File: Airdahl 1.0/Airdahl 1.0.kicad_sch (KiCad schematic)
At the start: 31 parts, among them J1 Conn_ARM_JTAG_SWD_20, SW1 SW_MEC_5E, U1 STM32F446RETx, X2 ABS25-32.768KHZ-6-T, Y1 ABM3B-8.000MHZ-12-D1X-T

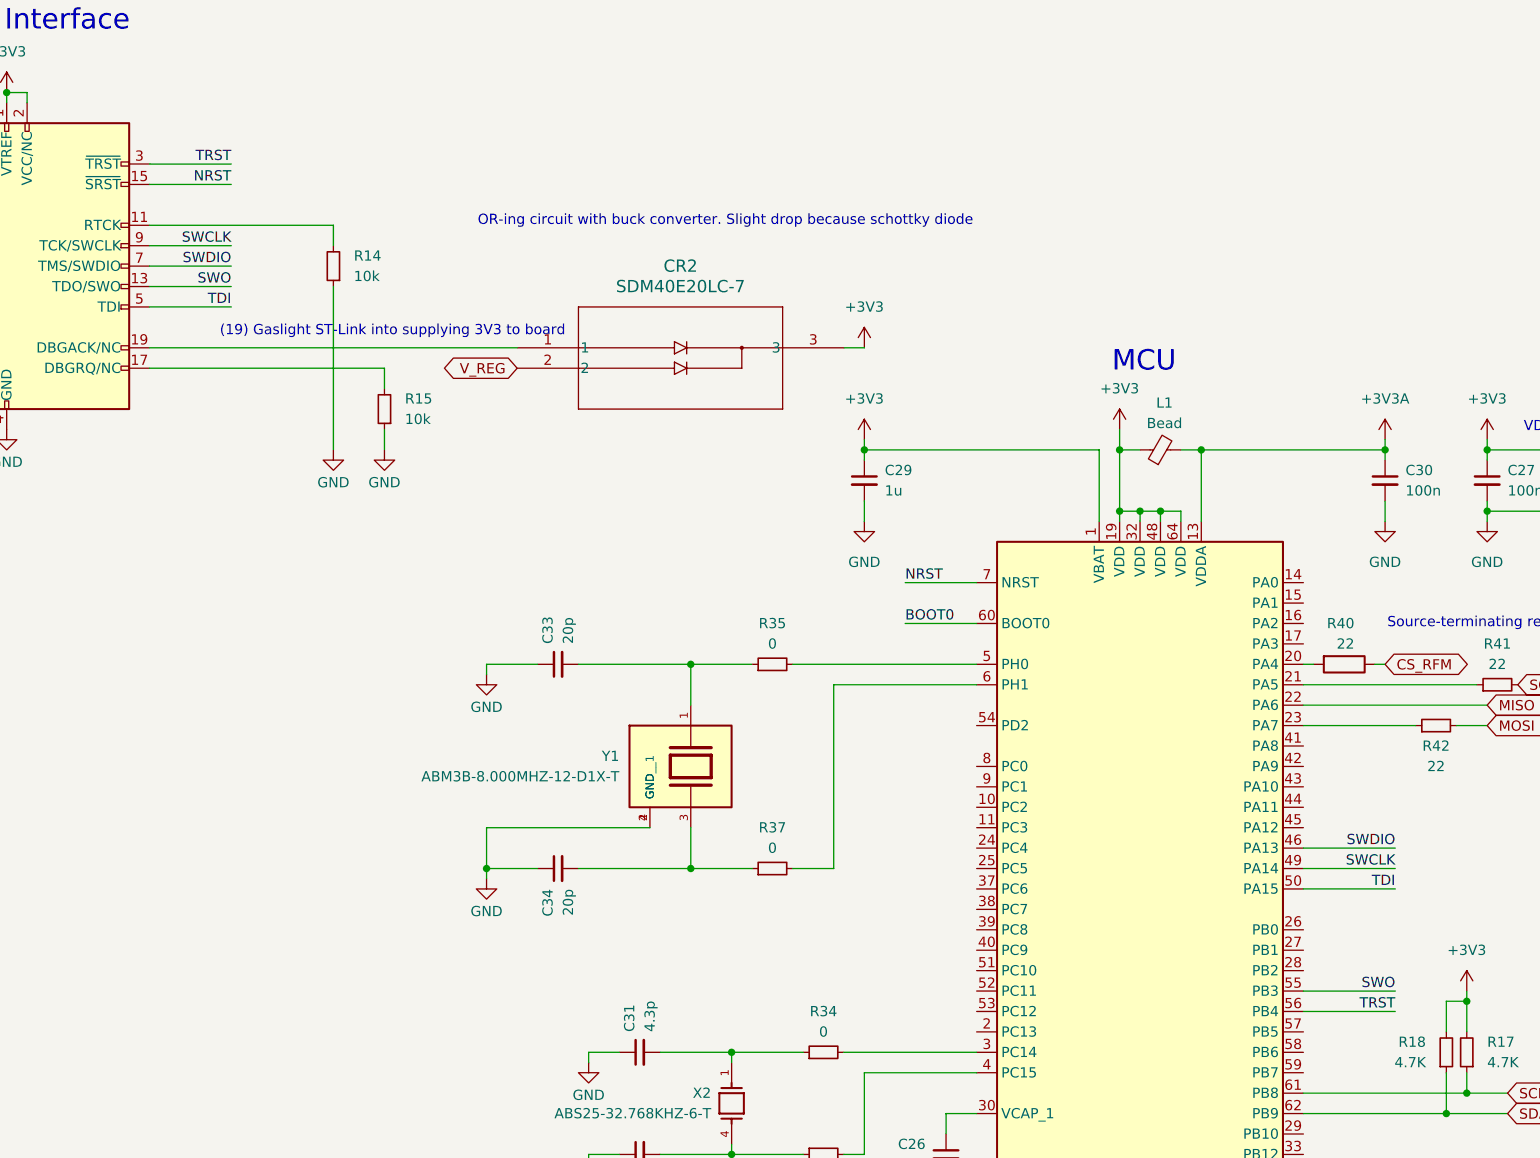
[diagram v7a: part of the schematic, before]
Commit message: added 5v buck, h bridge IC, updated jtag connections
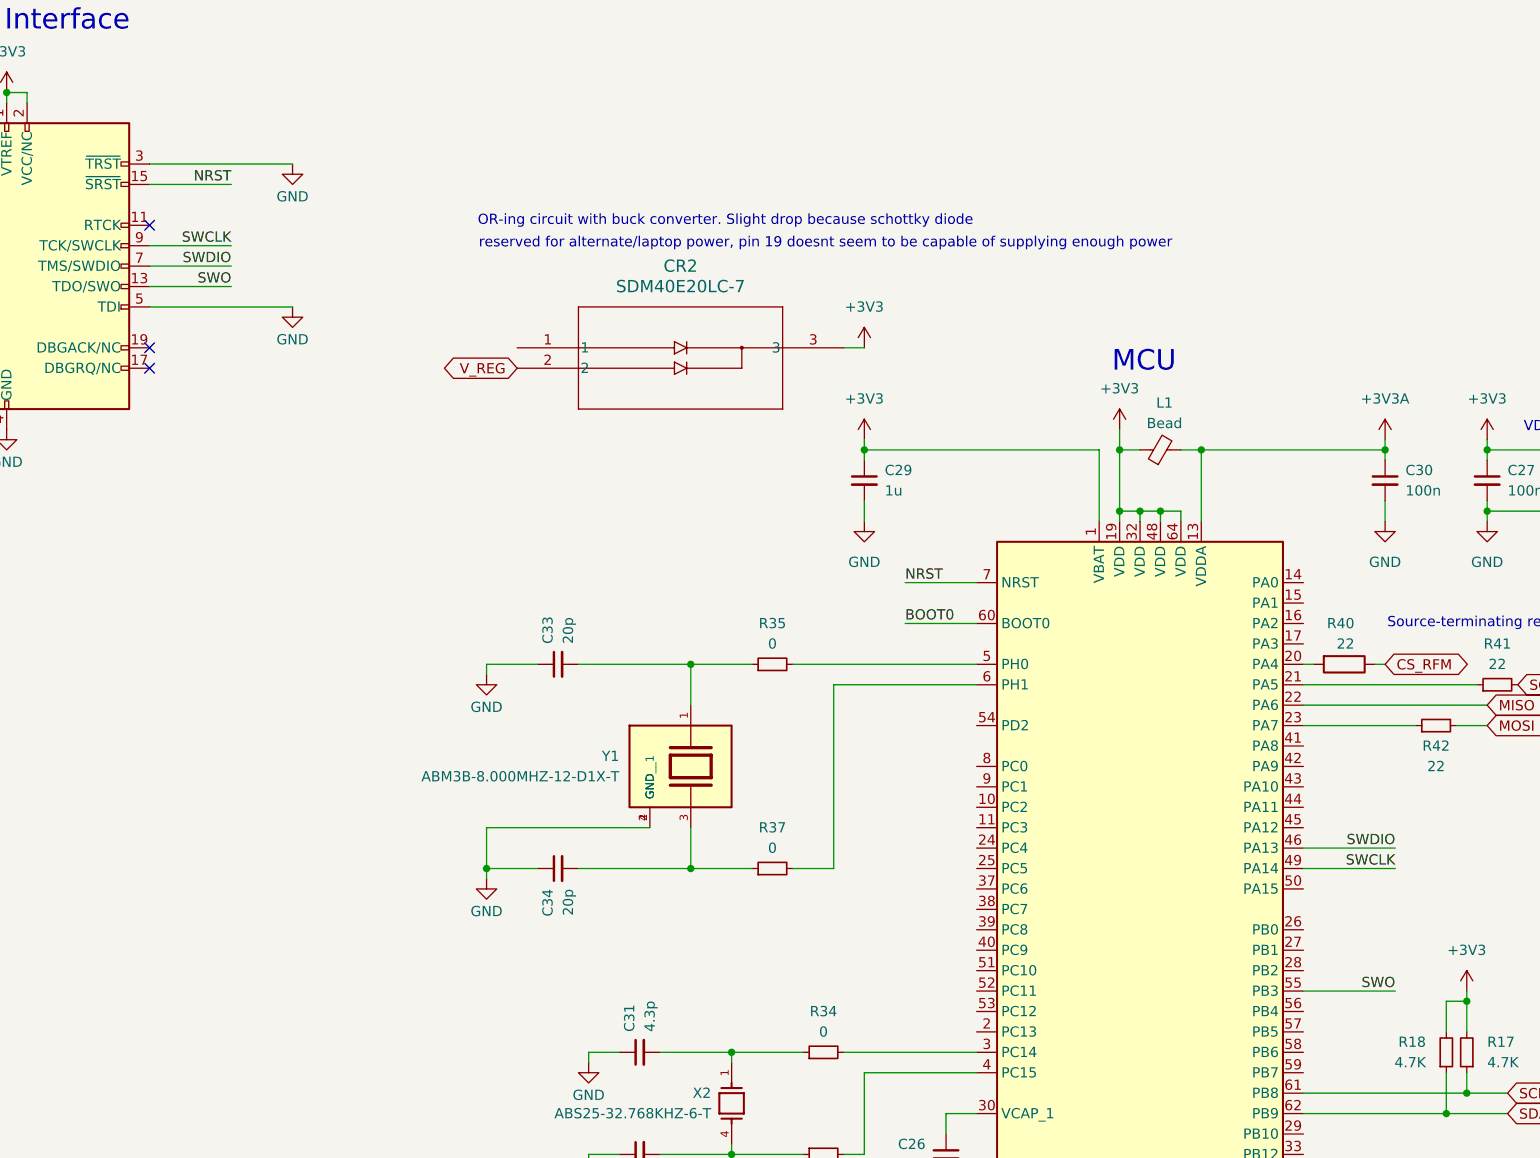
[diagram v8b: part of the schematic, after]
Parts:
- removed R14, R15: 10k, Resistor_SMD:R_0201_0603Metric_Pad0.64x0.40mm_HandSolder, symbol Device:R_Small
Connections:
- net GND: now also J1.3 (~{TRST}), J1.5 (TDI)
- net at CR2.1: no longer J1.19 (DBGACK/NC)
- net TDI: no longer names the net of U1.50 (PA15)
- net TDI: no longer J1.5 (TDI)
- net TRST: no longer names the net of U1.56 (PB4)
- net TRST: no longer J1.3 (~{TRST})
- no-connect marks 0 -> 3
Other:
- note added: "reserved for alternate/laptop power, pin 19 doesnt seem to be capable of supplying enough power"
- note removed: "(19) Gaslight ST-Link into supplying 3V3 to board"
